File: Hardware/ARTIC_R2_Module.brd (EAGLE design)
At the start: 20.3 x 33 mm, 146 parts, among them J25 U.FL, K1 TLP3475R, Q2 5.8A/30V/35mΩ, U1 ADM4210-1, U2 1.8V/100mA, U3 ARTIC_R2, U4 RFPA0133, U5 AS179-92LF, U6 3.0V, U7 SST25VF020BUSON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

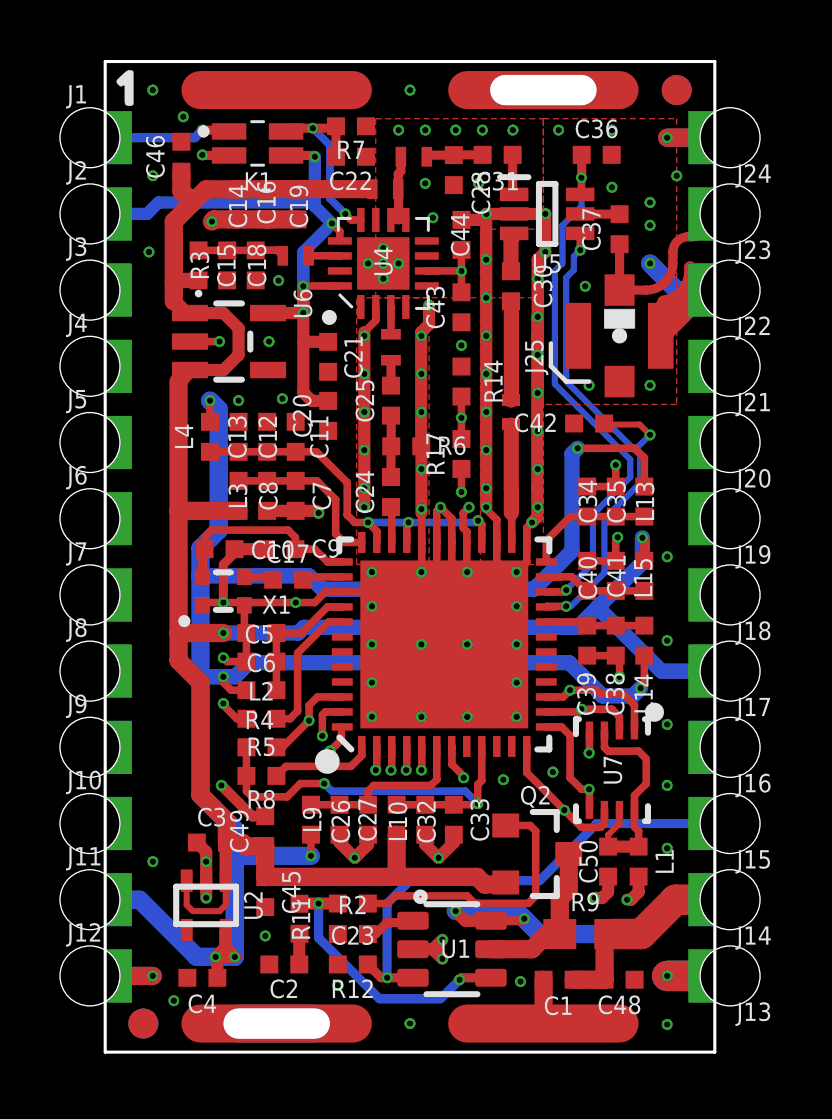
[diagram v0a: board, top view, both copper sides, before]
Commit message: Update Eagle files - remove New_Parts libraries
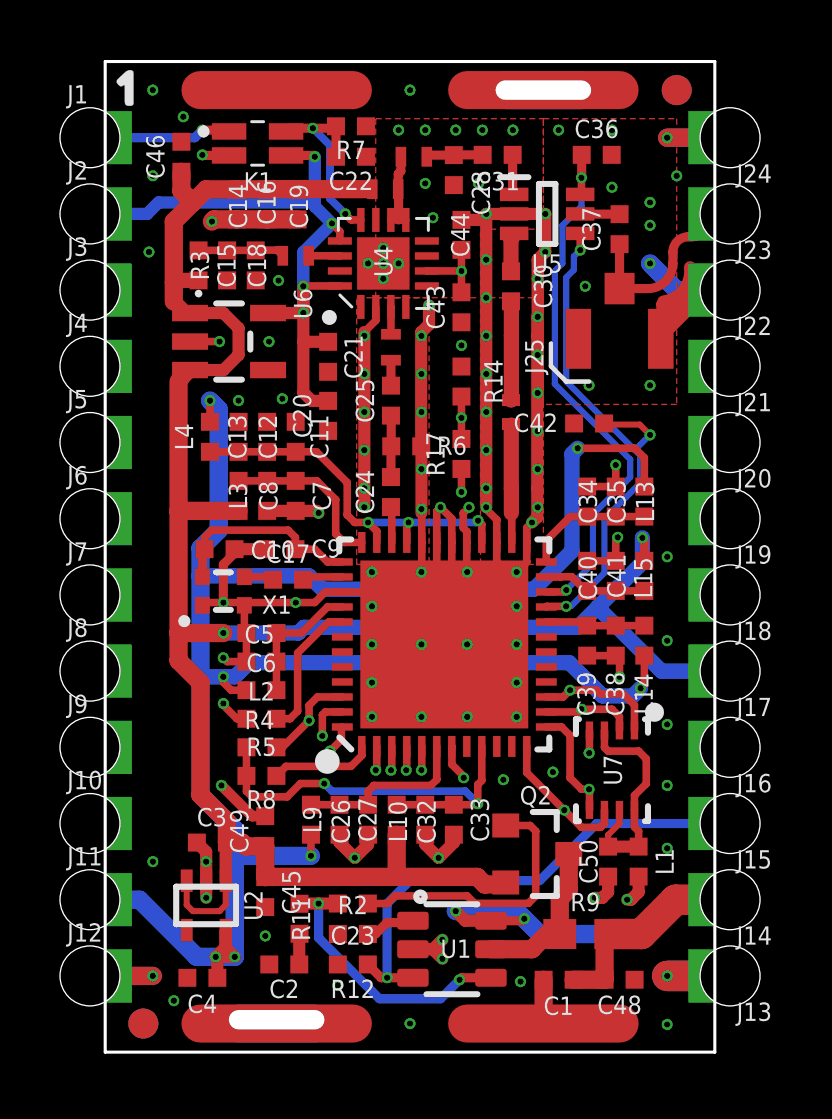
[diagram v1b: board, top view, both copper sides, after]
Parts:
- C28: device New_Parts_Capacitors:0402-TIGHT -> SparkFun-Capacitors:0402-TIGHT
- J25: device SparkFun-Connectors:U.FL -> SparkFun-Connectors:U.FL_REDUCED_FOOTPRINT
- K1: device New_Parts_DiscreteSemi:TLP3475RTPF -> SparkFun-DiscreteSemi:TLP3475RTPF
- L11, L12, L5, L6, L7, L8: device New_Parts_Coils:0402_COILCRAFT -> SparkFun-Coils:0402_COILCRAFT
- R11, R2: value 100OHM -> 100; device New_Parts_Resistors:0402-TIGHT -> SparkFun-Resistors:0402-TIGHT
- R14, R17: device New_Parts_Resistors:0402-TIGHT -> SparkFun-Resistors:0402-TIGHT
- R3: value 3.9OHM -> 3.9; device New_Parts_Resistors:0402-TIGHT -> SparkFun-Resistors:0402-TIGHT
- R6: value 220OHM -> 220; device New_Parts_Resistors:0402-TIGHT -> SparkFun-Resistors:0402-TIGHT
- R9: value 0.1R -> 0.1; device New_Parts_Resistors:0603 -> SparkFun-Resistors:0603
- SCREEN: value ARTIC_R2_CASTELLATED_CAN -> IOTA_SCREENING_CANSTRAIGHT_SLOTS; device New_Parts_Screening_Cans:ARTIC_R2_CASTELLATED -> New_Parts_Screening_Cans:IOTA_CAN_STRAIGHT_SLOTS
- U1: value ADM4210-1 -> ADM4210_1TSOT6; device New_Parts_IC-Power:TSOT6 -> SparkFun-IC-Power:TSOT6
- U3: device New_Parts_IC-Comms:QFN-48 -> SparkFun-RF:QFN-48
- U4: device New_Parts_IC-Comms:QFN50P300X300X86-17N -> SparkFun-RF:QFN50P300X300X86-17N
- U5: device New_Parts_IC-Comms:SOT65P220X100-6N -> SparkFun-RF:SOT65P220X100-6N
- U6: device New_Parts_IC-Power:SOT23-5 -> SparkFun-IC-Power:SOT23-5
- U7: device New_Parts_IC-Memory:USON_3X2MM -> SparkFun-IC-Memory:USON_3X2MM
- X1: device New_Parts_Clocks:CRYSTAL-TCXO-SMD-1.65X1.25 -> SparkFun-Clocks:CRYSTAL-TCXO-SMD-1.65X1.25
